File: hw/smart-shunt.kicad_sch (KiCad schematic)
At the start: 43 parts, among them J1 V supply, J2 V bus <80, J3 V bus >80, J4 Conn_01x01_Female, J5 Conn_01x01_Female, J6 GND, U1 XL7005A, U2 INA228, U3 ESP-12F

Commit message: finished pcb
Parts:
- removed D1: SS310, Diode_SMD:D_SMA_Handsoldering, symbol open-pe:SS310
- removed F?: Fuse_Small, symbol Device:Fuse_Small
- removed J1: V supply, TestPoint:TestPoint_Loop_D3.50mm_Drill0.9mm_Beaded, symbol Connector:Conn_01x01_Female
- removed J2: V bus <80, TestPoint:TestPoint_Loop_D3.50mm_Drill0.9mm_Beaded, symbol Connector:Conn_01x01_Female
- removed J3: V bus >80, TestPoint:TestPoint_Loop_D3.50mm_Drill0.9mm_Beaded, symbol Connector:Conn_01x01_Female
- removed J4, J5: Conn_01x01_Female, TestPoint:TestPoint_Loop_D3.50mm_Drill0.9mm_Beaded, symbol Connector:Conn_01x01_Female
- removed J6: GND, TestPoint:TestPoint_Loop_D3.50mm_Drill0.9mm_Beaded, symbol Connector:Conn_01x01_Female
- removed JP2: Jumper_2_Open, Jumper:SolderJumper-2_P1.3mm_Bridged2Bar_Pad1.0x1.5mm, symbol Jumper:Jumper_2_Open
- removed L1: 100uH, Inductor_SMD:L_Taiyo-Yuden_NR-60xx_HandSoldering, symbol Device:L
- removed R10: 33k, Resistor_SMD:R_0805_2012Metric, symbol Device:R_Small
- removed R8, R?: 10k, Resistor_SMD:R_0805_2012Metric, symbol Device:R_Small
- removed U1: XL7005A, Package_SO:SOIC-8_3.9x4.9mm_P1.27mm, symbol open-pe:XL7005A
- added C10: 1uF 100V, Capacitor_SMD:C_0805_2012Metric, symbol Device:C_Small
- added C11: 100nF, Capacitor_SMD:C_0805_2012Metric, symbol Device:C_Small
- added DZ1: D_Zener_Generic, symbol PCM_Diode_Zener_AKL:D_Zener_Generic
- added F2: Fuse_Small, Fuse:Fuseholder_Clip-5x20mm_Littelfuse_100_Inline_P20.50x4.60mm_D1.30mm_Horizontal, symbol Device:Fuse_Small
- added H1, H2, H3, H4: MountingHole, MountingHole:MountingHole_2.2mm_M2, symbol Mechanical:MountingHole
- added J1: Conn_01x03_Socket, Connector_PinHeader_2.54mm:PinHeader_1x03_P2.54mm_Vertical, symbol Connector:Conn_01x03_Socket
- added J10, J4, J9: Conn_01x02_Pin, Connector_PinHeader_2.54mm:PinHeader_1x02_P2.54mm_Vertical, symbol Connector:Conn_01x02_Pin
- added J2: UEXT_Slave, Connector_PinHeader_2.54mm:PinHeader_2x05_P2.54mm_Vertical, symbol Connector:UEXT_Slave
- added J3: UEXT_Slave2, Connector_PinHeader_2.54mm:PinHeader_2x05_P2.54mm_Vertical, symbol Connector:UEXT_Slave
- added J7, J8: Screw_Terminal_01x01, open-pe:Wuerth_PowerPlus_M5_Nut, symbol Connector:Screw_Terminal_01x01
- added JP2, JP4, JP5, JP6: SolderJumper_2_Open, PCM_Resistor_SMD_AKL:R_0402_1005Metric, symbol Jumper:SolderJumper_2_Open
- added JP3: Jumper_3_Open, Jumper:SolderJumper-3_P1.3mm_Open_RoundedPad1.0x1.5mm, symbol Jumper:Jumper_3_Open
- added L1: 22uH, Inductor_SMD:L_0805_2012Metric, symbol Device:L_Small
- added L2: LBR2012T101K, Inductor_SMD:L_0805_2012Metric, symbol Device:L
- added PS1: MIE1W0505BGLVH-3R-Z, open-pe:CONV_MIE1W0505BGLVH-3R-Z, symbol open-pe:MIE1W0505BGLVH-3R-Z
- added R18: R_Shunt, Resistor_SMD:R_Shunt_Isabellenhuette_BVR4026, symbol Device:R_Shunt
- added TH1, TH2: Thermistor_NTC, PCM_Resistor_SMD_AKL:R_0402_1005Metric, symbol Device:Thermistor_NTC
- added U1: TPT72616-SO1R, Package_SO:SOIC-8_3.9x4.9mm_P1.27mm, symbol Isolator:ISO1541
- added U4: TPT7721-SO1R, Package_SO:SOP-8_3.9x4.9mm_P1.27mm, symbol open-pe:TPT7721-SO1R
- C2: value 33nF -> 100nF
- C5: value 100uF -> 22uF; footprint Capacitor_SMD:CP_Elec_8x10 -> Capacitor_SMD:CP_Elec_6.3x5.9; MPN (none) -> A766EB226M1DLAE060
- C6, U3: now not fitted; now left out of the parts list
- C8, C9: renamed from C?; now not fitted; now left out of the parts list
- JP1: renamed from JP?; footprint (none) -> Jumper:SolderJumper-2_P1.3mm_Open_RoundedPad1.0x1.5mm
- R1, R2: footprint Resistor_SMD:R_0805_2012Metric -> Resistor_THT:R_Axial_DIN0204_L3.6mm_D1.6mm_P7.62mm_Horizontal
- R7: value 33k -> 10; footprint Resistor_SMD:R_0805_2012Metric -> PCM_Resistor_SMD_AKL:R_0805_2012Metric
- TP1, TP2, TP3: footprint TestPoint:TestPoint_Loop_D3.50mm_Drill0.9mm_Beaded -> TestPoint:TestPoint_Pad_D1.0mm
- gave numbers to parts that had none: 5
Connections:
- net +3.3V: now also D2.2 (A), J1.3 (Pin_3), J2.1 (3V3), JP4.2 (B), L2.1, PS1.5_6 (VOUT), U1.8 (VCC2), U4.8 (VCCB); no longer C3.1, C4.1, C8.1, C9.1, R7.1, U2.6 (VS)
- net Alert: now also R17.2, J2.3 (TXD), U4.7 (IN1)
- net GND: now also C2.2, C5.2, C10.1, DZ1.2 (A), F2.1, F2.2, J1.2 (Pin_2), J10.2 (Pin_2), J2.2 (GND), JP2.2 (B), PS1.2 (GND2), PS1.3_4 (GND2__1), PS1.7 (VSEL), U1.5 (GND2), U4.5 (GNDB); no longer U2.2 (A0)
- net SCL: now also J2.5 (SCL), JP6.2 (B), U1.6 (SCL2)
- net SDA: now also J2.6 (SDA), JP5.2 (B), U1.7 (SDA2)
- net Vbus: now also JP3.2 (C)
- net at R1.1, R2.2, R3.1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: now also JP3.1 (A)
- net Shunt-: now reaches R6.1
- net Shunt-: now also J9.2 (Pin_2), R18.3
- net at C7.1, R16.1, TP3.1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: now also DZ1.1 (K)
- net Vin: now reaches R7.2
- net Vin: now also R1.2, R3.2, J10.1 (Pin_1), JP3.3 (B); no longer C2.2
- net Shunt+: now reaches R5.1
- net Shunt+: now also J9.1 (Pin_1), R18.2
- new net: C3.1, C4.1, C8.1, C9.1, L2.2, U2.6 (VS)
- new net: J1.1 (Pin_1), L1.1
- new net: C10.2, L1.2, R7.1
- new net: J4.1 (Pin_1), TH1.1, TH2.1
- new net: J4.2 (Pin_2), TH1.2, TH2.2
- new net +3.3V2: C11.1, J3.1 (3V3), PS1.8 (EN), PS1.9_10 (VIN), U1.1 (VCC1), U4.1 (VCCA)
- new net A0: JP2.1 (A), JP4.1 (A), JP5.1 (A), JP6.1 (A), U2.2 (A0)
- new net Alert2: J3.3 (TXD), U4.2 (OUT1)
- new net GND2: C11.2, J3.2 (GND), PS1.1 (GND1), PS1.11_12 (GND1__1), U1.4 (GND1), U4.4 (GNDA)
- new net P+: J7.1 (Pin_1), R18.1
- new net P-: J8.1 (Pin_1), R18.4
- new net SCL2: J3.5 (SCL), U1.3 (SCL1)
- new net SDA2: J3.6 (SDA), U1.2 (SDA1)
- no-connect marks 0 -> 12
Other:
- note added: "close JP1 for HV ground-side measurement"
- note added: "use in-wire fuse"
- note removed: "5-80V input, 0.4 A load 150 KHz"
- moved on the sheet: C1, C3, C4, C7, D2, JP1, R1, R11, R12, R13, R15, R16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

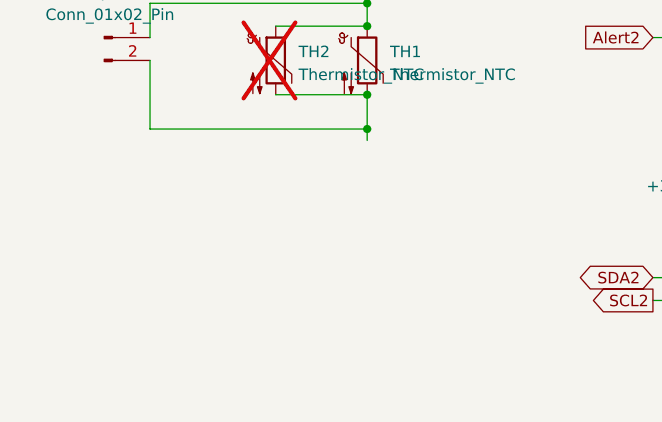
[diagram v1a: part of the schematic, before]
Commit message: add battery connector and LDO
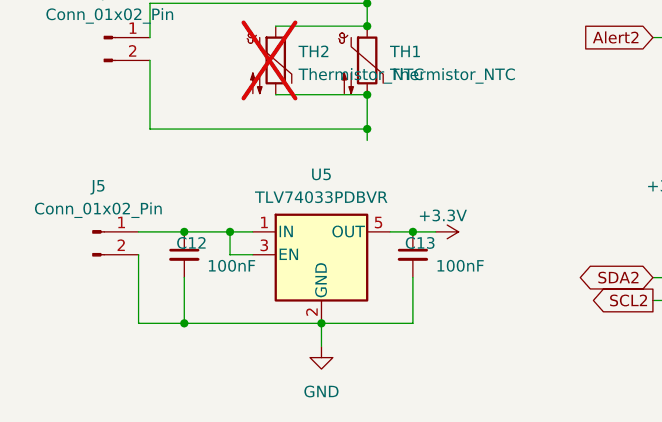
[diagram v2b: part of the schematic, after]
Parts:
- added C12, C13: 100nF, Capacitor_SMD:C_0805_2012Metric, symbol Device:C_Small
- added J5: Conn_01x02_Pin, Connector_PinHeader_2.54mm:PinHeader_1x02_P2.54mm_Vertical, symbol Connector:Conn_01x02_Pin
- added U5: TLV74033PDBVR, Package_TO_SOT_SMD:SOT-23-5, symbol Regulator_Linear:TLV70012_SOT23-5
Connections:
- net +3.3V: now also C13.1, U5.5 (OUT)
- net GND: now also C12.2, C13.2, J5.2 (Pin_2), U5.2 (GND)
- new net: C12.1, J5.1 (Pin_1), U5.1 (IN), U5.3 (EN)

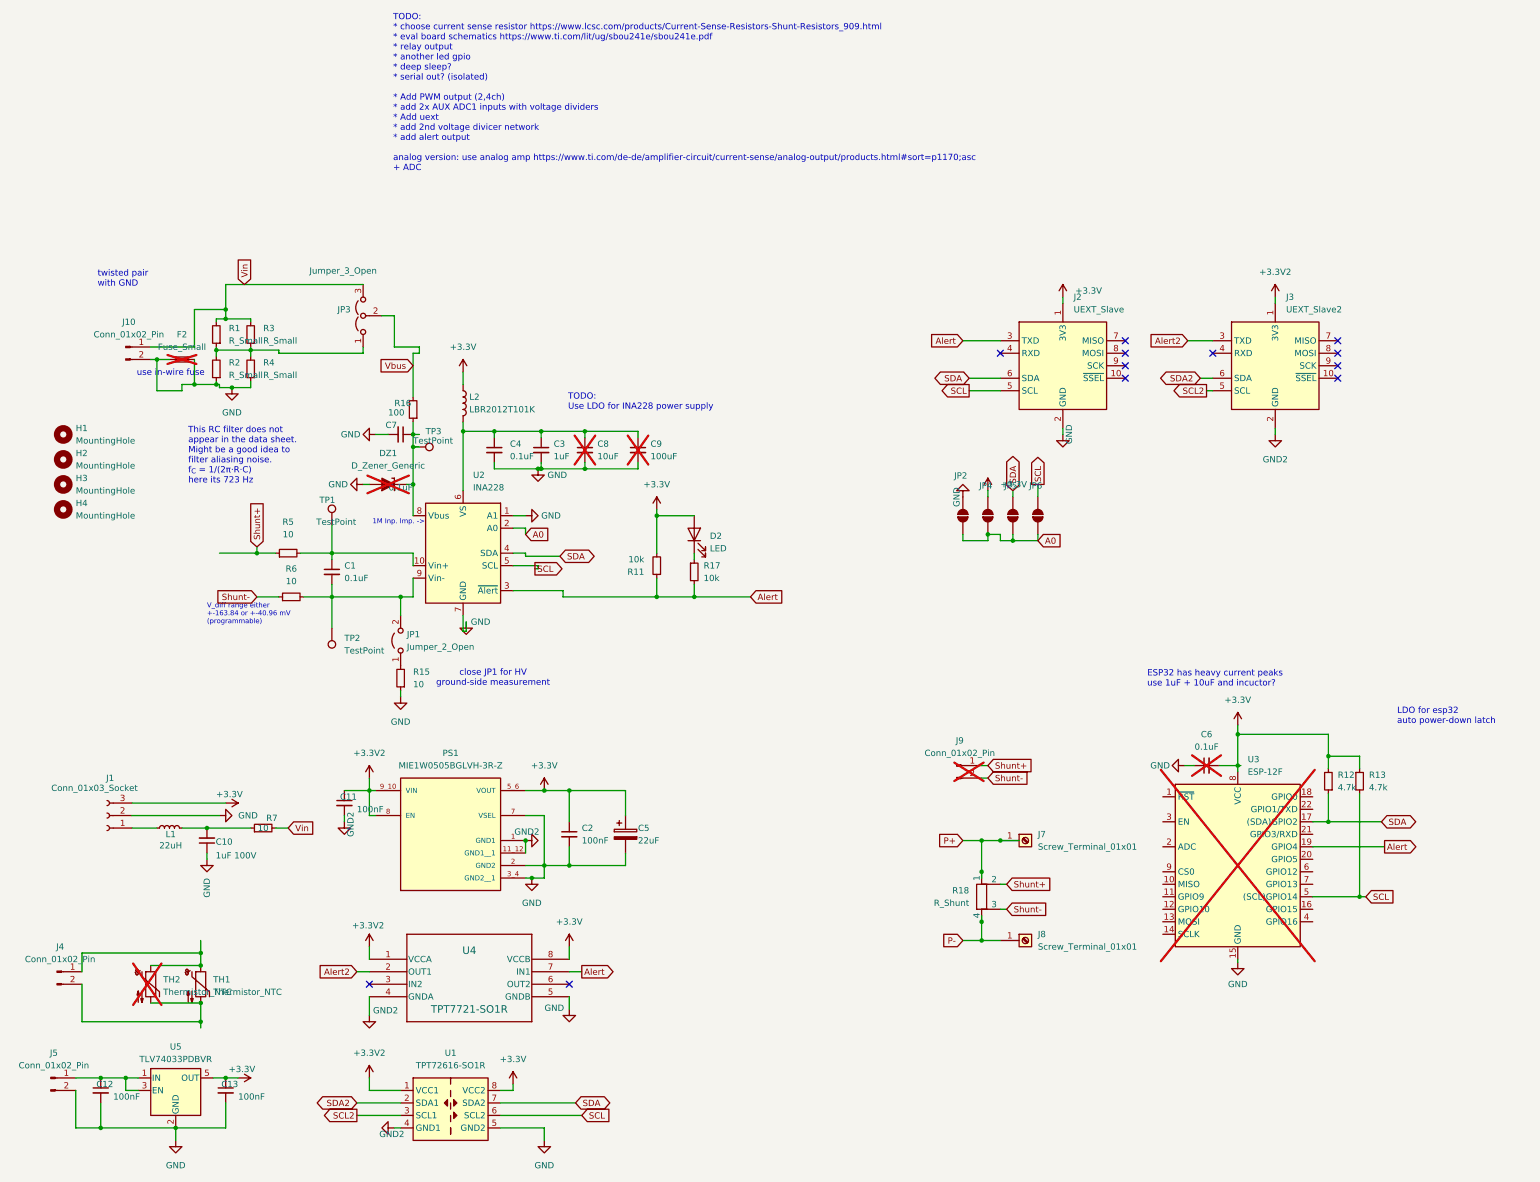
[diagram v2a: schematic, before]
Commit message: hw: 2nd LDO, mounting holes
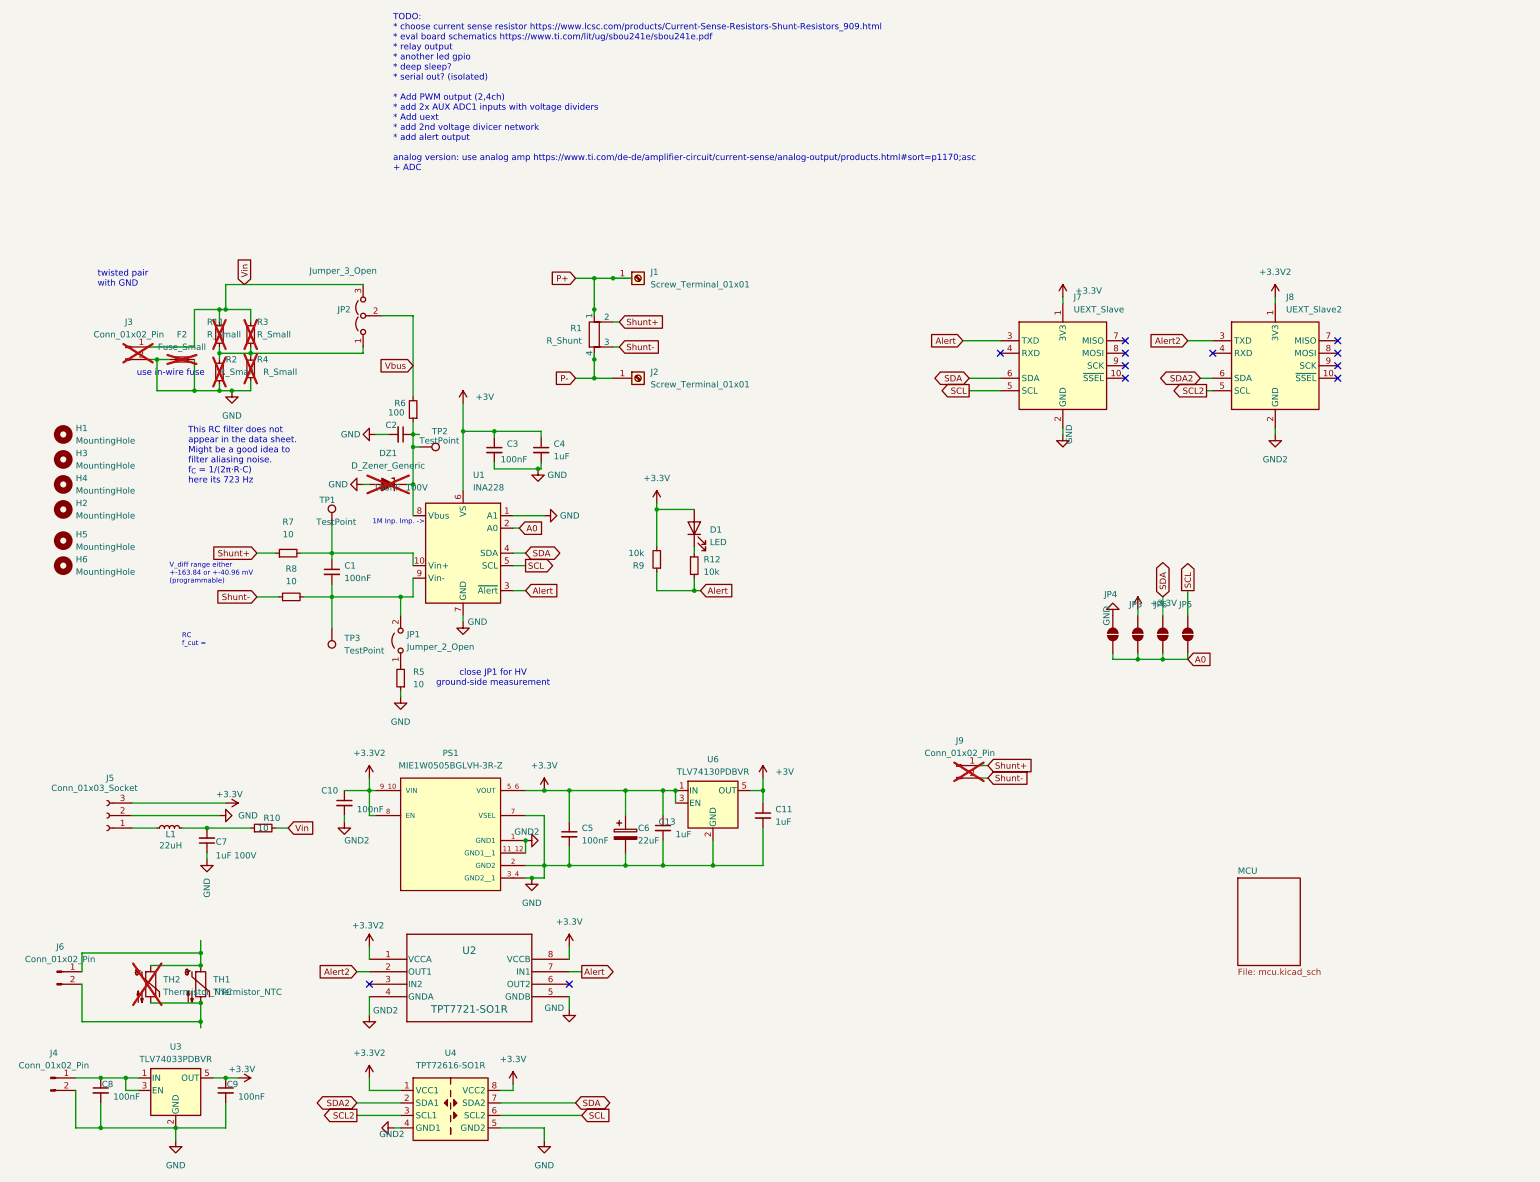
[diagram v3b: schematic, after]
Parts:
- removed C6: 0.1uF, Capacitor_SMD:C_0805_2012Metric, symbol Device:C_Small
- removed C8: 10uF, Capacitor_SMD:C_0805_2012Metric, symbol Device:C_Small
- removed C9: 100uF, Capacitor_SMD:C_0805_2012Metric, symbol Device:C_Small
- removed L2: LBR2012T101K, Inductor_SMD:L_0805_2012Metric, symbol Device:L
- removed R12, R13: 4.7k, Resistor_SMD:R_0805_2012Metric, symbol Device:R_Small
- removed U3: ESP-12F, RF_Module:ESP-12E, symbol open-pe:ESP-12F
- added C11, C13: 1uF, Capacitor_SMD:C_0805_2012Metric, symbol Device:C_Small
- added H5, H6: MountingHole, MountingHole:MountingHole_2.2mm_M2, symbol Mechanical:MountingHole
- added U6: TLV74130PDBVR, Package_TO_SOT_SMD:SOT-23-5, symbol Regulator_Linear:TLV70012_SOT23-5
- C1: value 0.1uF -> 100nF
- C2: renamed from C7; value 0.1uF -> 100nF, 100V
- C3: renamed from C4; value 0.1uF -> 100nF
- J3: renamed from J10; now not fitted; now left out of the parts list
- R11: renamed from R1; now not fitted; now left out of the parts list
- R2, R3, R4: now not fitted; now left out of the parts list
- renumbered C11 to C10, C3 to C4, C2 to C5, C5 to C6, C10 to C7, C12 to C8, C13 to C9, D2 to D1, H4 to H2, H2 to H3, H3 to H4, J7 to J1, J8 to J2, J5 to J4, J1 to J5, J4 to J6, J2 to J7, J3 to J8, JP3 to JP2, JP4 to JP3, JP2 to JP4, JP6 to JP5, JP5 to JP6, R18 to R1, R7 to R10, R17 to R12, R15 to R5, R16 to R6, R5 to R7, R6 to R8, R11 to R9, TP3 to TP2, TP2 to TP3, U2 to U1, U4 to U2, U5 to U3, U1 to U4
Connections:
- net +3.3V: now also C13.1, U6.1 (IN), U6.3 (EN)
- net GND: now also C11.2, C13.2, U6.2 (GND)
- net +3V: now reaches C3.1, C4.1, U1.6 (VS)
- net +3V: now also C11.1, U6.5 (OUT)
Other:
- added sheet MCU (mcu.kicad_sch)
- note added: "RC f_cut ="
- note removed: "ESP32 has heavy current peaks use 1uF + 10uF and incuctor?"
- note removed: "LDO for esp32 auto power-down latch"
- note removed: "TODO: Use LDO for INA228 power supply"
- moved on the sheet: D1, J1, J2, JP3, JP4, JP5, JP6, R1, R12, R9, TP2

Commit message: etc
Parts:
- added J10, J11: Conn_01x01, Connector_PinHeader_2.54mm:PinHeader_1x01_P2.54mm_Vertical, symbol Connector_Generic:Conn_01x01
- added JP7, JP8: Jumper_2_Open, open-pe:SolderJumper_0402_1005Metric, symbol Jumper:Jumper_2_Open
- added R15: WSK12161L000FEA, open-pe:SMT_61L000FEA_VIS, symbol Device:R_Shunt
- added R16: WSK12161L000FEA, open-pe:CSM3637_1-2mOHM_VIS, symbol Device:R_Shunt
- JP2: value Jumper_3_Open -> VbusSel
- JP3, JP4, JP5, JP6: footprint PCM_Resistor_SMD_AKL:R_0402_1005Metric -> open-pe:SolderJumper_0402_1005Metric
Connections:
- net P+: now also R15.4, R16.4
- net P-: now also R15.1, R16.1
- net Shunt+: now also J10.1 (Pin_1), JP7.2 (B); no longer R1.2
- net Shunt-: now also J11.1 (Pin_1), JP8.2 (B); no longer R1.3
- new net: JP7.1 (A), R1.2, R15.3, R16.3
- new net: JP8.1 (A), R1.3, R15.2, R16.2
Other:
- moved on the sheet: F2, J1, J2, J3, R1, R11, R2, R3, R4, R6

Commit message: add riedon rsn footprint, copper only path
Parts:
- added C14: 10uF, Capacitor_SMD:C_0805_2012Metric, symbol Device:C_Small
- added J12: Riedon RSN, open-pe:RiedonRSN, symbol Connector:Screw_Terminal_01x02
- JP7, JP8: footprint open-pe:SolderJumper_0402_1005Metric -> open-pe:SolderJumper_0402_1005Metric_Bridged; symbol Jumper:Jumper_2_Open -> Jumper:Jumper_2_Bridged
- R6: value 100 -> 10
- R7, R8: footprint Resistor_SMD:R_0805_2012Metric -> open-pe:R_0805_2012Metric_Bridged
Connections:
- net +3.3V2: now also C14.1
- net GND2: now also C14.2
- net Shunt+: now also J12.1 (Pin_1)
- net Shunt-: now also J12.2 (Pin_2)
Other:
- moved on the sheet: C10, C7, J5, L1, R10
